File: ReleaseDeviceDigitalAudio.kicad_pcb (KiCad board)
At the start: 2 copper layers, 132 x 68.5 mm, 184 parts, among them IC1 ULN2003F12FN-7, IC2 ULN2003F12FN-7, IC3 ULN2003F12FN-7, IC4 ULN2003F12FN-7, J1 AudioJack3, J10 UIBoardCON1, J11 SignalStrength, J12 KeySwitch, J2 AudioJack3, J3 AudioJack3, J4 AudioJack3, J5 AudioJack3, J6 UIBoardCON2, J7 BAT, J8 IGNITION, J9 ATMEGA_PROG, Q2 SQ2362ES-T1_GE3, Q3 SQD50P06-15L_GE3, Q4 SQJ461EP-T1-GE3, U1 PCF85063A, U10 VOMA617A, U11 VOMA617A, U12 LM53635LQRNL*Q1, U13 TLVH431AQDBVRQ1, U14 LM74610-Q1, U15 ATmega4809-A, U2 BM83SM1-00TA, U3 SN74LV1T126, U4 SN74LV1T126, U6 MAX98089ETN+, U7 CD4514BM, U8 CD4511BPWR, U9 Compute_Module_4_Connectors, Y1 9HT12, Y2 830208220101

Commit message: - Libs hinzugefügt / merge fertig
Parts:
- removed J12: KeySwitch, Connector_PinHeader_2.54mm:PinHeader_1x03_P2.54mm_Vertical
- added SW1: KeySwitch, TeKaDe:KeySwitch, F.Cu at (219.3, 46.1)
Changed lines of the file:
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@@
     (add_net VPP)
+  )
+  (module TeKaDe:KeySwitch (layer F.Cu)
+    (at 219.255 46.061)
+    (fp_text reference SW1 (at 14.5 -32) (layer F.SilkS)
+      (effects (font (size 1 1) (thickness 0.15)))
+    )
+    (fp_text value KeySwitch (at 6.5 -32) (layer F.Fab)
+      (effects (font (size 1 1) (thickness 0.15)))
+    )
+    (fp_text user "Lock Area" (at 9 -13.5) (layer F.SilkS)
+      (effects (font (size 1 1) (thickness 0.15)))
+    )
+    (fp_line (start 0 0) (end 17 0) (layer F.SilkS) (width 0.12))
+    (fp_line (start 17 0) (end 17 -12) (layer F.SilkS) (width 0.12))
+    (fp_line (start 17 -12) (end 18.5 -12) (layer F.SilkS) (width 0.12))
+    (fp_line (start 18.5 -12) (end 18.5 -24.5) (layer F.SilkS) (width 0.12))
+    (fp_line (start 18.5 -24.5) (end 18.5 -30) (layer F.SilkS) (width 0.12))
+    (fp_line (start 18.5 -30) (end 0 -30) (layer F.SilkS) (width 0.12))
+    (fp_line (start 0 -30) (end 0 0) (layer F.SilkS) (width 0.12))
+    (fp_line (start 18.5 -24.5) (end 0 -24.5) (layer F.SilkS) (width 0.12))
+    (pad 3 thru_hole circle (at 16.5 -28.5) (size 1.524 1.524) (drill 0.762) (layers *.Cu *.Mask)
+      (net 2 GND))
+    (pad 2 thru_hole circle (at 11 -28.5) (size 1.524 1.524) (drill 0.762) (layers *.Cu *.Mask)
+      (net 139 /ControllerUIBoard/KeySwitchB))
+    (pad 1 thru_hole circle (at 5.5 -28.5) (size 1.524 1.524) (drill 0.762) (layers *.Cu *.Mask)
+      (net 140 /ControllerUIBoard/KeySwitchA))
   )
   (module MountingHole:MountingHole_2.5mm locked (layer F.Cu)
@@
       (at (xyz 0 0 0))
       (scale (xyz 1 1 1))
-      (rotate (xyz 0 0 0))
-    )
-  )
-  (module Connector_PinHeader_2.54mm:PinHeader_1x03_P2.54mm_Vertical (layer F.Cu)
-    (at -29.79 116.4)
-    (descr "Through hole straight pin header, 1x03, 2.54mm pitch, single row")
-    (tags "Through hole pin header THT 1x03 2.54mm single row")
-    (fp_text reference J12 (at 0 -2.33) (layer F.SilkS)
-      (effects (font (size 1 1) (thickness 0.15)))
-    )
-    (fp_text value KeySwitch (at 0 7.41) (layer F.Fab)
-      (effects (font (size 1 1) (thickness 0.15)))
-    )
-    (fp_text user %R (at 0 2.54 90) (layer F.Fab)
-      (effects (font (size 1 1) (thickness 0.15)))
-    )
-    (fp_line (start 1.8 -1.8) (end -1.8 -1.8) (layer F.CrtYd) (width 0.05))
-    (fp_line (start 1.8 6.85) (end 1.8 -1.8) (layer F.CrtYd) (width 0.05))
-    (fp_line (start -1.8 6.85) (end 1.8 6.85) (layer F.CrtYd) (width 0.05))
-    (fp_line (start -1.8 -1.8) (end -1.8 6.85) (layer F.CrtYd) (width 0.05))
-    (fp_line (start -1.33 -1.33) (end 0 -1.33) (layer F.SilkS) (width 0.12))
-    (fp_line (start -1.33 0) (end -1.33 -1.33) (layer F.SilkS) (width 0.12))
-    (fp_line (start -1.33 1.27) (end 1.33 1.27) (layer F.SilkS) (width 0.12))
-    (fp_line (start 1.33 1.27) (end 1.33 6.41) (layer F.SilkS) (width 0.12))
-    (fp_line (start -1.33 1.27) (end -1.33 6.41) (layer F.SilkS) (width 0.12))
-    (fp_line (start -1.33 6.41) (end 1.33 6.41) (layer F.SilkS) (width 0.12))
-    (fp_line (start -1.27 -0.635) (end -0.635 -1.27) (layer F.Fab) (width 0.1))
-    (fp_line (start -1.27 6.35) (end -1.27 -0.635) (layer F.Fab) (width 0.1))
-    (fp_line (start 1.27 6.35) (end -1.27 6.35) (layer F.Fab) (width 0.1))
-    (fp_line (start 1.27 -1.27) (end 1.27 6.35) (layer F.Fab) (width 0.1))
-    (fp_line (start -0.635 -1.27) (end 1.27 -1.27) (layer F.Fab) (width 0.1))
-    (pad 3 thru_hole oval (at 0 5.08) (size 1.7 1.7) (drill 1) (layers *.Cu *.Mask)
-      (net 2 GND))
-    (pad 2 thru_hole oval (at 0 2.54) (size 1.7 1.7) (drill 1) (layers *.Cu *.Mask)
-      (net 139 /ControllerUIBoard/KeySwitchB))
-    (pad 1 thru_hole rect (at 0 0) (size 1.7 1.7) (drill 1) (layers *.Cu *.Mask)
-      (net 140 /ControllerUIBoard/KeySwitchA))
-    (model ${KISYS3DMOD}/Connector_PinHeader_2.54mm.3dshapes/PinHeader_1x03_P2.54mm_Vertical.wrl
-      (at (xyz 0 0 0))
-      (scale (xyz 1 1 1))

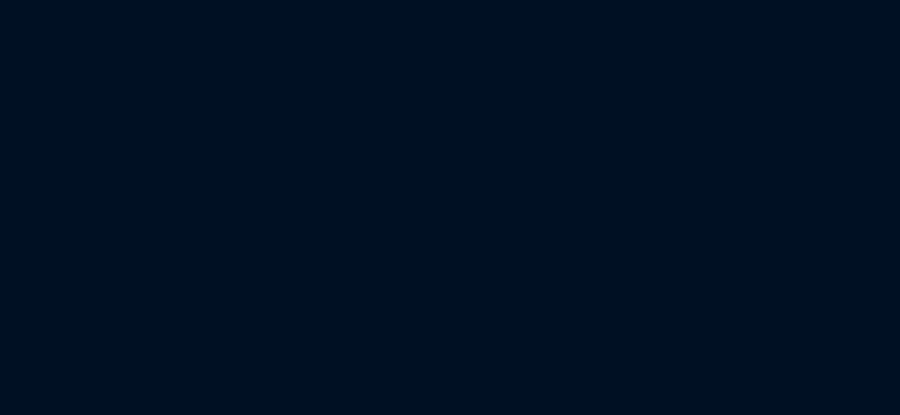
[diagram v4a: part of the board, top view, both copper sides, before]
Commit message: [mod:] socket pin mirroring
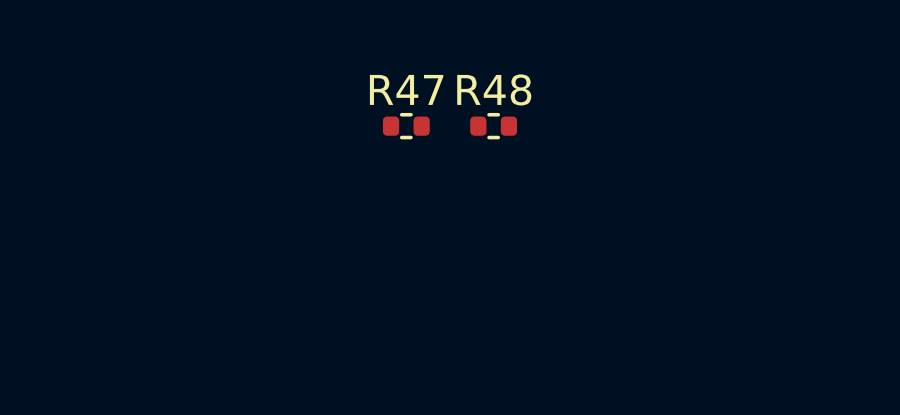
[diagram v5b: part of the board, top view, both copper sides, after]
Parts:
- added R47: 100R/1%, Resistor_SMD:R_0402_1005Metric, F.Cu at (236.1, -162.1)
- added R48: 47k/5%, Resistor_SMD:R_0402_1005Metric, F.Cu at (239.0, -162.1)
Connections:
- net Net-(J6-Pad30) renamed /7SegmentDriver/5V_BL_SUPPLY
- J10 pad 1: /ControllerUIBoard/LDR -> /ControllerUIBoard/LED_YL
- J10 pad 10: /ControllerUIBoard/DataEncoderDataOutB -> /ControllerUIBoard/DataEncoderDataOutC
- J10 pad 11: /ControllerUIBoard/DataEncoderDataOutA -> +5V
- J10 pad 12: +5V -> /ControllerUIBoard/DataEncoderDataOutA
- J10 pad 13: /ControllerUIBoard/LED_ON -> +5V
- J10 pad 14: +5V -> /ControllerUIBoard/LED_ON
- J10 pad 15: /ControllerUIBoard/DataEncoderDataOutE -> /ControllerUIBoard/DataEncoderDataOutD
- J10 pad 16: /ControllerUIBoard/DataEncoderDataOutD -> /ControllerUIBoard/DataEncoderDataOutE
- J10 pad 2: /ControllerUIBoard/LED_YL -> /ControllerUIBoard/LDR
- J10 pad 3: /ControllerUIBoard/LED_GN -> /ControllerUIBoard/LED_RD
- J10 pad 4: /ControllerUIBoard/LED_RD -> /ControllerUIBoard/LED_GN
- J10 pad 5: Net-(J10-Pad5) -> /ControllerUIBoard/ButtonA2GND
- J10 pad 6: /ControllerUIBoard/ButtonA2GND -> Net-(J10-Pad6)
- J10 pad 7: /ControllerUIBoard/DataEncoderDataAvailable -> /ControllerUIBoard/DataEncoderOutputEnable
- J10 pad 8: /ControllerUIBoard/DataEncoderOutputEnable -> /ControllerUIBoard/DataEncoderDataAvailable
- J10 pad 9: /ControllerUIBoard/DataEncoderDataOutC -> /ControllerUIBoard/DataEncoderDataOutB
- J6 pad 1: /7SegmentDriver/SegmentFAnode -> /7SegmentDriver/SegmentEAnode
- J6 pad 10: Net-(J6-Pad10) -> /7SegmentDriver/CathodeDigit14
- J6 pad 11: /7SegmentDriver/CathodeDigit8 -> /7SegmentDriver/CathodeDigit7
- J6 pad 12: /7SegmentDriver/CathodeDigit7 -> /7SegmentDriver/CathodeDigit8
- J6 pad 13: /7SegmentDriver/CathodeDigit10 -> /7SegmentDriver/CathodeDigit9
- J6 pad 14: /7SegmentDriver/CathodeDigit9 -> /7SegmentDriver/CathodeDigit10
- J6 pad 15: /7SegmentDriver/CathodeDigit12 -> /7SegmentDriver/CathodeDigit11
- J6 pad 16: /7SegmentDriver/CathodeDigit11 -> /7SegmentDriver/CathodeDigit12
- J6 pad 17: /7SegmentDriver/CathodeDigit6 -> /7SegmentDriver/CathodeDigit13
- J6 pad 18: /7SegmentDriver/CathodeDigit13 -> /7SegmentDriver/CathodeDigit6
- J6 pad 19: /7SegmentDriver/CathodeDigitA -> /7SegmentDriver/CathodeDigitB
- J6 pad 2: /7SegmentDriver/SegmentEAnode -> /7SegmentDriver/SegmentFAnode
- J6 pad 20: /7SegmentDriver/CathodeDigitB -> /7SegmentDriver/CathodeDigitA
- J6 pad 21: /7SegmentDriver/CathodeDigit1 -> /7SegmentDriver/CathodeDigit2
- J6 pad 22: /7SegmentDriver/CathodeDigit2 -> /7SegmentDriver/CathodeDigit1
- J6 pad 23: /7SegmentDriver/CathodeDigit3 -> /7SegmentDriver/CathodeDigit4
- J6 pad 24: /7SegmentDriver/CathodeDigit4 -> /7SegmentDriver/CathodeDigit3
- J6 pad 25: /7SegmentDriver/CathodeDigit5 -> Net-(J6-Pad25)
- J6 pad 26: Net-(J6-Pad26) -> /7SegmentDriver/CathodeDigit5
- J6 pad 27: GND -> Net-(J6-Pad27)
- J6 pad 28: Net-(J6-Pad28) -> GND
- J6 pad 29: +5V -> Net-(J6-Pad29)
- J6 pad 3: /7SegmentDriver/SegmentBAnode -> /7SegmentDriver/SegmentAAnode
- J6 pad 4: /7SegmentDriver/SegmentAAnode -> /7SegmentDriver/SegmentBAnode
- J6 pad 5: /7SegmentDriver/SegmentGAnode -> /7SegmentDriver/SegmentDAnode
- J6 pad 6: /7SegmentDriver/SegmentDAnode -> /7SegmentDriver/SegmentGAnode
- J6 pad 7: Net-(J6-Pad7) -> /7SegmentDriver/SegmentCAnode
- J6 pad 8: /7SegmentDriver/SegmentCAnode -> Net-(J6-Pad8)
- J6 pad 9: /7SegmentDriver/CathodeDigit14 -> Net-(J6-Pad9)
- U2 pad 5: Net-(U2-Pad5) -> /AudioMAX98089/MCLK
- U6 pad 5: /AudioMAX98089/MAX_MCLK -> /AudioMAX98089/MCLK

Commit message: - Schaltbare BL Versorgung fertig - kleinere Value Anpassungen - Finale Annotation
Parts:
- removed the C27 at (116.9, -41.2)
- removed the J7 at (-33.8, 155.7)
- removed the J8 at (-48.8, 167.8)
- removed Y2: 830208220101, TeKaDe:WE_IQXO-791
- added J9: Conn_01x03, TerminalBlock_Phoenix:TerminalBlock_Phoenix_MKDS-1,5-3_1x03_P5.00mm_Horizontal, F.Cu at (-73.7, 172.8)
- added Q1: Q_PMOS_GSD, Package_TO_SOT_SMD:SOT-23, F.Cu at (232.7, 119.5)
- moved R15 277.4 mm to (231.1, 115.3)
- moved R16 277.4 mm to (234.0, 115.3)
- renumbered C77 to C1, C56 to C10, C57 to C11, C58 to C12, C59 to C13, C60 to C14, C61 to C15, C62 to C16, C63 to C17, C64 to C18, C65 to C19, C78 to C2, C66 to C20, C67 to C21, C68 to C22, C69 to C23, C70 to C24, C71 to C25, C72 to C26, C73 to C27, C74 to C28, C75 to C29, C79 to C3, C76 to C30, C44 to C31, C45 to C32, C46 to C33, C47 to C34, C48 to C35, C49 to C36, C50 to C37, C41 to C38, C42 to C39, C80 to C4, C43 to C40, C10 to C41, C11 to C42, C12 to C43, C13 to C44, C14 to C45, C15 to C46, C16 to C47, C17 to C48, C18 to C49, C51 to C5, C19 to C50, C20 to C51, C21 to C52, C22 to C53, C23 to C54, C24 to C55, C25 to C56, C26 to C57, C28 to C58, C29 to C59, C52 to C6, C30 to C60, C31 to C61, C32 to C62, C33 to C63, C34 to C64, C35 to C65, C36 to C66, C37 to C67, C38 to C68, C39 to C69, C53 to C7, C40 to C70, C7 to C71, C8 to C72, C2 to C73, C3 to C74, C4 to C75, C5 to C76, C6 to C77, C1 to C78, C54 to C8, C55 to C9, D5 to D1, D3 to D10, D1 to D11, D6 to D2, D7 to D3, D8 to D4, D9 to D5, D10 to D6, D11 to D7, D4 to D8, D2 to D9, H7 to H5, H8 to H6, J6 to J10, J9 to J6, J11 to J7, J10 to J8, L3 to L1, L1 to L2, L2 to L3, Q2 to Q3, Q3 to Q4, Q4 to Q5, R33 to R1, R42 to R10, R43 to R11, R44 to R12, R45 to R13, R46 to R14, R47 to R15, R48 to R16, R20 to R17, R21 to R18, R22 to R19, R34 to R2, R23 to R20, R24 to R21, R25 to R22, R26 to R23, R27 to R24, R28 to R25, R29 to R26, R30 to R27, R31 to R28, R32 to R29, R36 to R3, R11 to R30, R12 to R31, R13 to R32, R14 to R33, R15 to R34, R16 to R35, R17 to R36, R18 to R37, R19 to R38, R10 to R39, R35 to R4, R5 to R40, R6 to R41, R7 to R42, R8 to R43, R9 to R44, R1 to R45, R2 to R46, R3 to R47, R4 to R48, R37 to R5, R38 to R6, R39 to R7, R40 to R8, R41 to R9, U15 to U1, IC1 to U10, IC2 to U11, IC3 to U12, IC4 to U13, U6 to U14, U3 to U15, U4 to U16, U2 to U17, U1 to U18, U10 to U2, U11 to U3, U12 to U4, U13 to U5, U14 to U6, U9 to U7, U7 to U8, U8 to U9
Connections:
- net /7SegmentDriver/SegmentAAnode renamed /7SegmentDriver/AnodeSegmentA
- net /7SegmentDriver/SegmentBAnode renamed /7SegmentDriver/AnodeSegmentB
- net /7SegmentDriver/SegmentCAnode renamed /7SegmentDriver/AnodeSegmentC
- net /7SegmentDriver/SegmentDAnode renamed /7SegmentDriver/AnodeSegmentD
- net /7SegmentDriver/SegmentEAnode renamed /7SegmentDriver/AnodeSegmentE
- net /7SegmentDriver/SegmentFAnode renamed /7SegmentDriver/AnodeSegmentF
- net /7SegmentDriver/SegmentGAnode renamed /7SegmentDriver/AnodeSegmentG
- net Net-(C54-Pad1) renamed /PowerSupply/IGNITION
- R15 pad 1: Net-(Q5-Pad1) (its old number) -> Net-(Q1-Pad1)
- R16 pad 1: Net-(Q5-Pad1) (its old number) -> +5V
- R16 pad 2: GND -> Net-(Q1-Pad1)

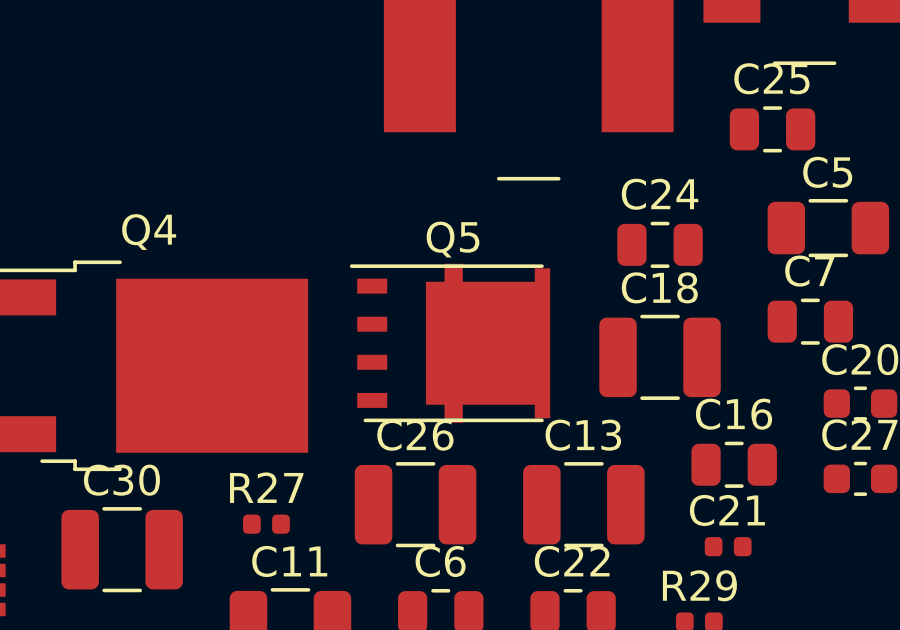
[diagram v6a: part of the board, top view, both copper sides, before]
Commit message: - Bauteile konsolidiert
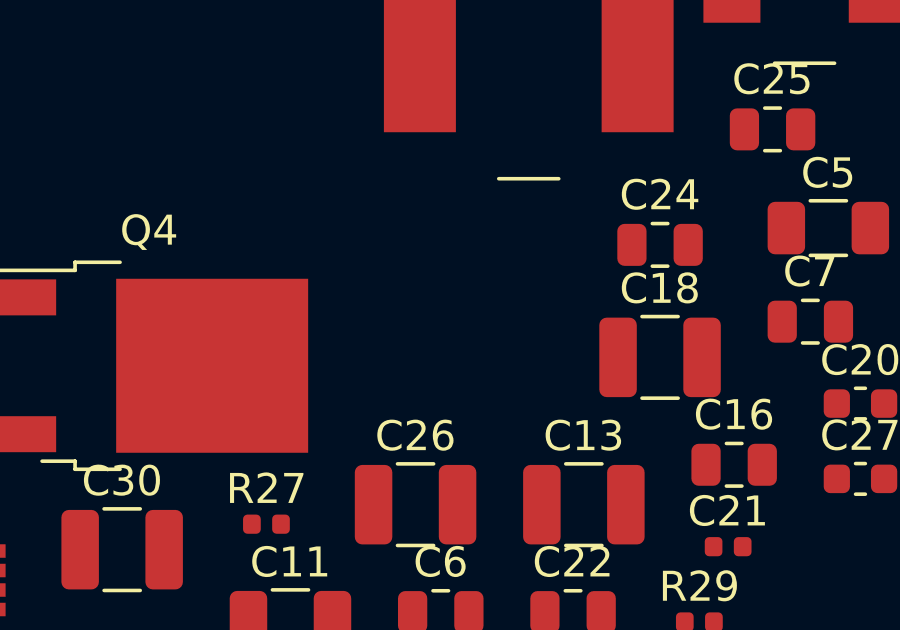
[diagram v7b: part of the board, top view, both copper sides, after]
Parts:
- removed Q5: SQJ461EP-T1-GE3, TeKaDe:PowerPAK-SO-8L-SINGLE
- C35, C36: value 22u/6V3/X5R -> 22u/10V/X5R
- Q1: value Q_PMOS_GSD -> BSS314PEH6327XTSA1
- R12, R19: value 100k/5% -> 100k/1%
- R16: value 47k/5% -> 47k/1%
- R29: value 20k/5% -> 20k/1%
- R44, R45: value 10k/5% -> 10k/1%

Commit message: - fix: footprint getauscht
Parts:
- U9: footprint Package_SO:TSSOP-14_4.4x5mm_P0.65mm -> Package_SO:TSSOP-16_4.4x5mm_P0.65mm
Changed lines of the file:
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@@
     (add_net VPP)
+  )
+  (module Package_SO:TSSOP-16_4.4x5mm_P0.65mm (layer F.Cu)
+    (at 323.27 106.09)
+    (descr "16-Lead Plastic Thin Shrink Small Outline (ST)-4.4 mm Body [TSSOP] (see Microchip Packaging Specification 00000049BS.pdf)")
+    (tags "SSOP 0.65")
+    (attr smd)
+    (fp_text reference U9 (at 0 -3.55) (layer F.SilkS)
+      (effects (font (size 1 1) (thickness 0.15)))
+    )
+    (fp_text value CD4511BPWR (at 0 3.55) (layer F.Fab)
+      (effects (font (size 1 1) (thickness 0.15)))
+    )
+    (fp_text user %R (at 0 0) (layer F.Fab)
+      (effects (font (size 0.8 0.8) (thickness 0.15)))
+    )
+    (fp_line (start -3.775 -2.8) (end 2.2 -2.8) (layer F.SilkS) (width 0.15))
+    (fp_line (start -2.2 2.725) (end 2.2 2.725) (layer F.SilkS) (width 0.15))
+    (fp_line (start -3.95 2.8) (end 3.95 2.8) (layer F.CrtYd) (width 0.05))
+    (fp_line (start -3.95 -2.9) (end 3.95 -2.9) (layer F.CrtYd) (width 0.05))
+    (fp_line (start 3.95 -2.9) (end 3.95 2.8) (layer F.CrtYd) (width 0.05))
+    (fp_line (start -3.95 -2.9) (end -3.95 2.8) (layer F.CrtYd) (width 0.05))
+    (fp_line (start -2.2 -1.5) (end -1.2 -2.5) (layer F.Fab) (width 0.15))
+    (fp_line (start -2.2 2.5) (end -2.2 -1.5) (layer F.Fab) (width 0.15))
+    (fp_line (start 2.2 2.5) (end -2.2 2.5) (layer F.Fab) (width 0.15))
+    (fp_line (start 2.2 -2.5) (end 2.2 2.5) (layer F.Fab) (width 0.15))
+    (fp_line (start -1.2 -2.5) (end 2.2 -2.5) (layer F.Fab) (width 0.15))
+    (pad 16 smd rect (at 2.95 -2.275) (size 1.5 0.45) (layers F.Cu F.Paste F.Mask)
+      (net 1 +5V))
+    (pad 15 smd rect (at 2.95 -1.625) (size 1.5 0.45) (layers F.Cu F.Paste F.Mask)
+      (net 129 /7SegmentDriver/AnodeSegmentF))
+    (pad 14 smd rect (at 2.95 -0.975) (size 1.5 0.45) (layers F.Cu F.Paste F.Mask)
+      (net 125 /7SegmentDriver/AnodeSegmentG))
+    (pad 13 smd rect (at 2.95 -0.325) (size 1.5 0.45) (layers F.Cu F.Paste F.Mask)
+      (net 128 /7SegmentDriver/AnodeSegmentA))
+    (pad 12 smd rect (at 2.95 0.325) (size 1.5 0.45) (layers F.Cu F.Paste F.Mask)
+      (net 127 /7SegmentDriver/AnodeSegmentB))
+    (pad 11 smd rect (at 2.95 0.975) (size 1.5 0.45) (layers F.Cu F.Paste F.Mask)
+      (net 124 /7SegmentDriver/AnodeSegmentC))
+    (pad 10 smd rect (at 2.95 1.625) (size 1.5 0.45) (layers F.Cu F.Paste F.Mask)
+      (net 126 /7SegmentDriver/AnodeSegmentD))
+    (pad 9 smd rect (at 2.95 2.275) (size 1.5 0.45) (layers F.Cu F.Paste F.Mask)
+      (net 130 /7SegmentDriver/AnodeSegmentE))
+    (pad 8 smd rect (at -2.95 2.275) (size 1.5 0.45) (layers F.Cu F.Paste F.Mask)
+      (net 2 GND))
+    (pad 7 smd rect (at -2.95 1.625) (size 1.5 0.45) (layers F.Cu F.Paste F.Mask)
+      (net 117 /7SegmentDriver/7Seg_Driver_A))
+    (pad 6 smd rect (at -2.95 0.975) (size 1.5 0.45) (layers F.Cu F.Paste F.Mask)
+      (net 118 /7SegmentDriver/7Seg_Driver_D))
+    (pad 5 smd rect (at -2.95 0.325) (size 1.5 0.45) (layers F.Cu F.Paste F.Mask)
+      (net 2 GND))
+    (pad 4 smd rect (at -2.95 -0.325) (size 1.5 0.45) (layers F.Cu F.Paste F.Mask)
+      (net 23 "Net-(C39-Pad1)"))
+    (pad 3 smd rect (at -2.95 -0.975) (size 1.5 0.45) (layers F.Cu F.Paste F.Mask)
+      (net 1 +5V))
+    (pad 2 smd rect (at -2.95 -1.625) (size 1.5 0.45) (layers F.Cu F.Paste F.Mask)
+      (net 119 /7SegmentDriver/7Seg_Driver_C))
+    (pad 1 smd rect (at -2.95 -2.275) (size 1.5 0.45) (layers F.Cu F.Paste F.Mask)
+      (net 120 /7SegmentDriver/7Seg_Driver_B))
+    (model ${KISYS3DMOD}/Package_SO.3dshapes/TSSOP-16_4.4x5mm_P0.65mm.wrl
+      (at (xyz 0 0 0))
+      (scale (xyz 1 1 1))
+      (rotate (xyz 0 0 0))
+    )
   )
   (module TerminalBlock_Phoenix:TerminalBlock_Phoenix_MKDS-1,5-3_1x03_P5.00mm_Horizontal (layer F.Cu)
@@
       (at (xyz 0 0 0))
       (scale (xyz 1 1 1))
-      (rotate (xyz 0 0 0))
-    )
-  )
-  (module Package_SO:TSSOP-14_4.4x5mm_P0.65mm (layer F.Cu)
-    (at 323.27 106.09)
-    (descr "14-Lead Plastic Thin Shrink Small Outline (ST)-4.4 mm Body [TSSOP] (see Microchip Packaging Specification 00000049BS.pdf)")
-    (tags "SSOP 0.65")
-    (attr smd)
-    (fp_text reference U9 (at 0 -3.55) (layer F.SilkS)
-      (effects (font (size 1 1) (thickness 0.15)))
-    )
-    (fp_text value CD4511BPWR (at 0 3.55) (layer F.Fab)
-      (effects (font (size 1 1) (thickness 0.15)))
-    )
-    (fp_line (start -1.2 -2.5) (end 2.2 -2.5) (layer F.Fab) (width 0.15))
-    (fp_line (start 2.2 -2.5) (end 2.2 2.5) (layer F.Fab) (width 0.15))
-    (fp_line (start 2.2 2.5) (end -2.2 2.5) (layer F.Fab) (width 0.15))
-    (fp_line (start -2.2 2.5) (end -2.2 -1.5) (layer F.Fab) (width 0.15))
-    (fp_line (start -2.2 -1.5) (end -1.2 -2.5) (layer F.Fab) (width 0.15))
-    (fp_line (start -3.95 -2.8) (end -3.95 2.8) (layer F.CrtYd) (width 0.05))
-    (fp_line (start 3.95 -2.8) (end 3.95 2.8) (layer F.CrtYd) (width 0.05))
-    (fp_line (start -3.95 -2.8) (end 3.95 -2.8) (layer F.CrtYd) (width 0.05))
-    (fp_line (start -3.95 2.8) (end 3.95 2.8) (layer F.CrtYd) (width 0.05))
-    (fp_line (start -2.325 -2.625) (end -2.325 -2.5) (layer F.SilkS) (width 0.15))
-    (fp_line (start 2.325 -2.625) (end 2.325 -2.4) (layer F.SilkS) (width 0.15))
-    (fp_line (start 2.325 2.625) (end 2.325 2.4) (layer F.SilkS) (width 0.15))
-    (fp_line (start -2.325 2.625) (end -2.325 2.4) (layer F.SilkS) (width 0.15))
-    (fp_line (start -2.325 -2.625) (end 2.325 -2.625) (layer F.SilkS) (width 0.15))
-    (fp_line (start -2.325 2.625) (end 2.325 2.625) (layer F.SilkS) (width 0.15))
-    (fp_line (start -2.325 -2.5) (end -3.675 -2.5) (layer F.SilkS) (width 0.15))
-    (fp_text user %R (at 0 0) (layer F.Fab)
-      (effects (font (size 0.8 0.8) (thickness 0.15)))
-    )
-    (pad 14 smd rect (at 2.95 -1.95) (size 1.45 0.45) (layers F.Cu F.Paste F.Mask)
-      (net 125 /7SegmentDriver/AnodeSegmentG))
-    (pad 13 smd rect (at 2.95 -1.3) (size 1.45 0.45) (layers F.Cu F.Paste F.Mask)
-      (net 128 /7SegmentDriver/AnodeSegmentA))
-    (pad 12 smd rect (at 2.95 -0.65) (size 1.45 0.45) (layers F.Cu F.Paste F.Mask)
-      (net 127 /7SegmentDriver/AnodeSegmentB))
-    (pad 11 smd rect (at 2.95 0) (size 1.45 0.45) (layers F.Cu F.Paste F.Mask)
-      (net 124 /7SegmentDriver/AnodeSegmentC))
-    (pad 10 smd rect (at 2.95 0.65) (size 1.45 0.45) (layers F.Cu F.Paste F.Mask)
-      (net 126 /7SegmentDriver/AnodeSegmentD))
-    (pad 9 smd rect (at 2.95 1.3) (size 1.45 0.45) (layers F.Cu F.Paste F.Mask)
-      (net 130 /7SegmentDriver/AnodeSegmentE))
-    (pad 8 smd rect (at 2.95 1.95) (size 1.45 0.45) (layers F.Cu F.Paste F.Mask)
-      (net 2 GND))
-    (pad 7 smd rect (at -2.95 1.95) (size 1.45 0.45) (layers F.Cu F.Paste F.Mask)
-      (net 117 /7SegmentDriver/7Seg_Driver_A))
-    (pad 6 smd rect (at -2.95 1.3) (size 1.45 0.45) (layers F.Cu F.Paste F.Mask)
-      (net 118 /7SegmentDriver/7Seg_Driver_D))
-    (pad 5 smd rect (at -2.95 0.65) (size 1.45 0.45) (layers F.Cu F.Paste F.Mask)
-      (net 2 GND))
-    (pad 4 smd rect (at -2.95 0) (size 1.45 0.45) (layers F.Cu F.Paste F.Mask)
-      (net 23 "Net-(C39-Pad1)"))
-    (pad 3 smd rect (at -2.95 -0.65) (size 1.45 0.45) (layers F.Cu F.Paste F.Mask)
-      (net 1 +5V))
-    (pad 2 smd rect (at -2.95 -1.3) (size 1.45 0.45) (layers F.Cu F.Paste F.Mask)
-      (net 119 /7SegmentDriver/7Seg_Driver_C))
-    (pad 1 smd rect (at -2.95 -1.95) (size 1.45 0.45) (layers F.Cu F.Paste F.Mask)
-      (net 120 /7SegmentDriver/7Seg_Driver_B))
-    (model ${KISYS3DMOD}/Package_SO.3dshapes/TSSOP-14_4.4x5mm_P0.65mm.wrl
-      (at (xyz 0 0 0))
-      (scale (xyz 1 1 1))
